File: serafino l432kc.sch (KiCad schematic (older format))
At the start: 31 parts, among them J1 USB_B_Micro, J2 Conn_01x14, J3 Conn_01x14, Q1 SI3401A-TP, SW1 SW_Push, SW2 SW_Push, U1 AP2112K-3.3, U2 USBLC6-2SC6, U3 STM32L432KCUx, Y1 32.768K

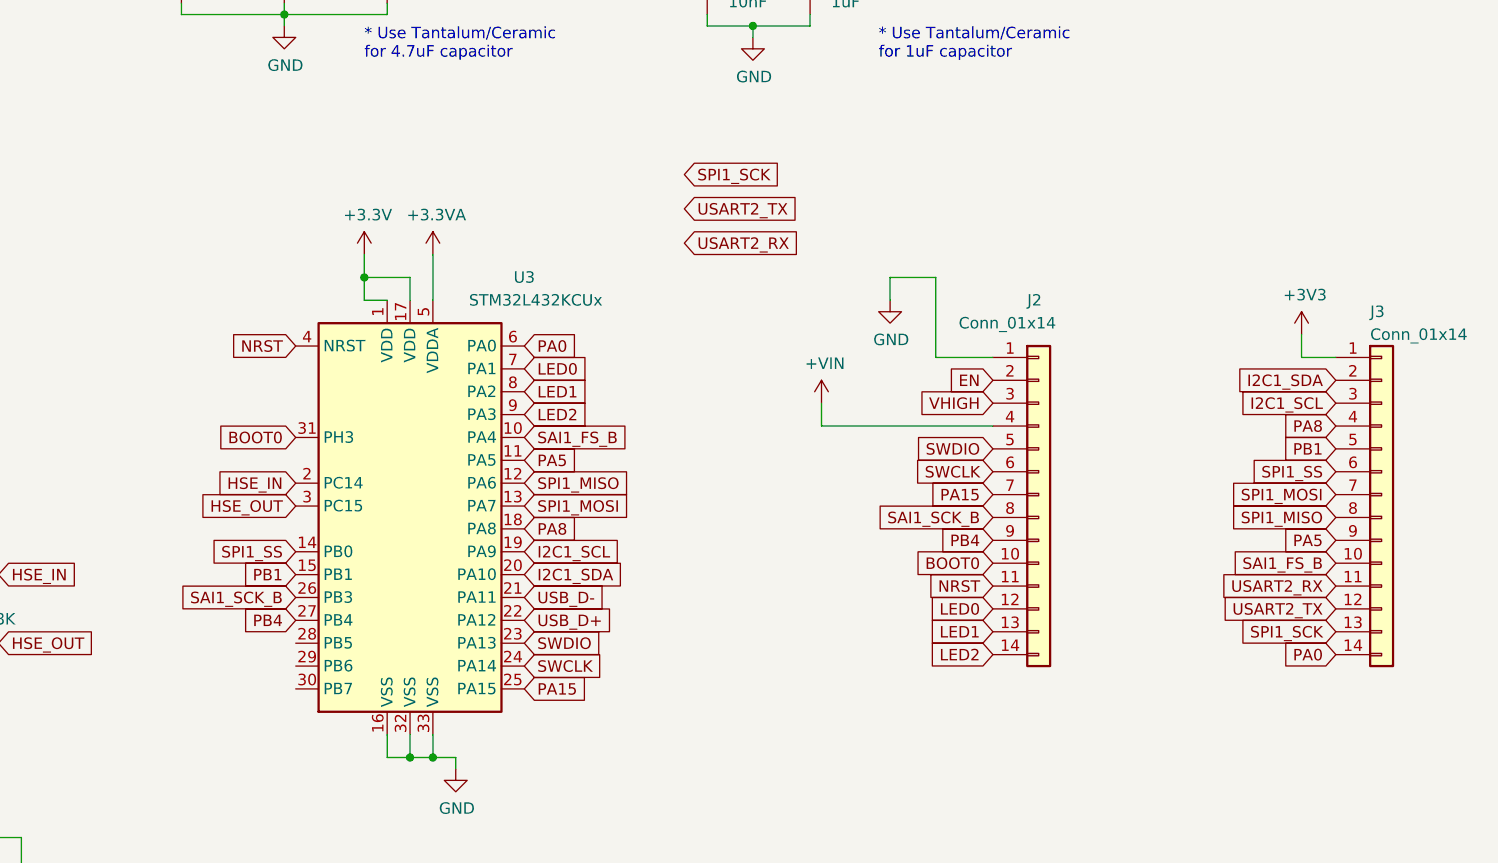
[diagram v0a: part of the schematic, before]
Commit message: PWM Leds
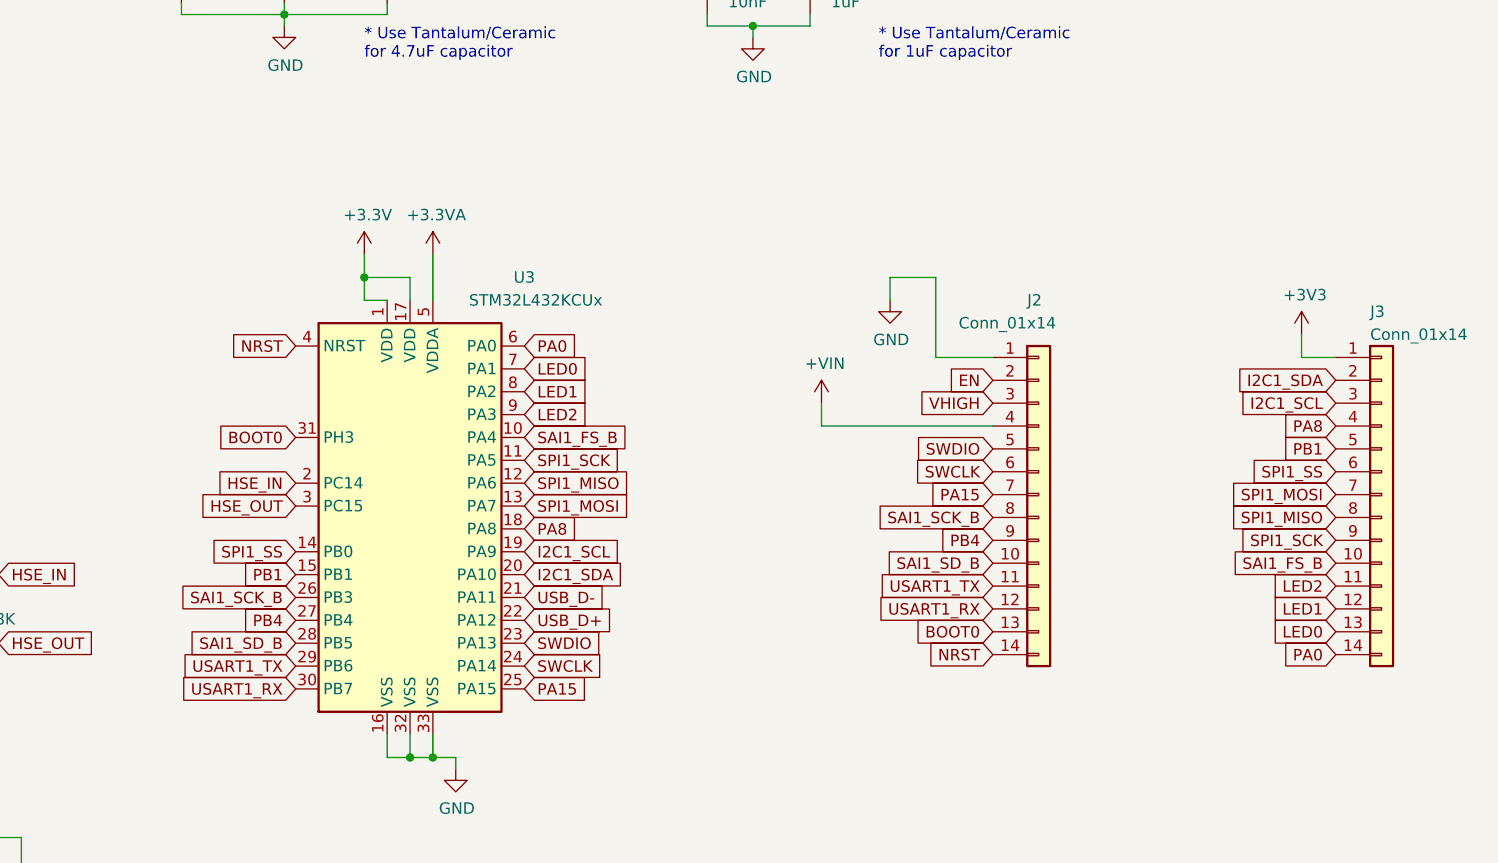
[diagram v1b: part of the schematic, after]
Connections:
- net PA5 is gone; now on net SPI1_SCK: J3.9 (Pin_9), U3.11 (PA5)
- net USART2_RX is gone; now on net LED2: J3.11 (Pin_11)
- net USART2_TX is gone; now on net LED1: J3.12 (Pin_12)
- net BOOT0: now also J2.13 (Pin_13); no longer J2.10 (Pin_10)
- net LED0: now also J3.13 (Pin_13); no longer J2.12 (Pin_12)
- net LED1: no longer J2.13 (Pin_13)
- net LED2: no longer J2.14 (Pin_14)
- net NRST: now also J2.14 (Pin_14); no longer J2.11 (Pin_11)
- net SPI1_SCK: no longer J3.13 (Pin_13)
- net SAI1_SD_B: now reaches U3.28 (PB5)
- net SAI1_SD_B: now also J2.10 (Pin_10)
- net USART1_TX: now reaches U3.29 (PB6)
- net USART1_TX: now also J2.11 (Pin_11)
- net USART1_RX: now reaches U3.30 (PB7)
- net USART1_RX: now also J2.12 (Pin_12)
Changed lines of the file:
@@
 Text GLabel 6700 4500 2    50   Input ~ 0
 USB_D-
-Text GLabel 7400 2800 2    50   Input ~ 0
-USART2_TX
-Text GLabel 7400 2950 2    50   Input ~ 0
-USART2_RX
+Text GLabel 5700 4800 0    50   Input ~ 0
+USART1_TX
+Text GLabel 5700 4900 0    50   Input ~ 0
+USART1_RX
 Text Notes 5200 1400 0    50   ~ 0
 VDD Decouples
@@
 Text GLabel 6700 4100 2    50   Input ~ 0
 SPI1_MOSI
-Text GLabel 7400 2650 2    50   Input ~ 0
+Text GLabel 6700 3900 2    50   Input ~ 0
 SPI1_SCK
 Text GLabel 6700 4000 2    50   Input ~ 0
@@
 Text GLabel 8750 3650 0    50   Input ~ 0
 VHIGH
-Text GLabel 8750 4450 0    50   Input ~ 0
+Text GLabel 8750 4750 0    50   Input ~ 0
 NRST
 Text GLabel 10250 3750 0    50   Input ~ 0
@@
 Text GLabel 8750 4250 0    50   Input ~ 0
 PB4
-Text GLabel 8750 4550 0    50   Input ~ 0
+Text GLabel 10250 4650 0    50   Input ~ 0
 LED0
-Text GLabel 8750 4650 0    50   Input ~ 0
+Text GLabel 10250 4550 0    50   Input ~ 0
 LED1
-Text GLabel 8750 4750 0    50   Input ~ 0
+Text GLabel 10250 4450 0    50   Input ~ 0
 LED2
 Text GLabel 10250 4050 0    50   Input ~ 0
@@
 Text GLabel 10250 4150 0    50   Input ~ 0
 SPI1_MISO
-Text GLabel 10250 4250 0    50   Input ~ 0
-PA5
 Text GLabel 10250 4350 0    50   Input ~ 0
 SAI1_FS_B
-Text GLabel 10250 4450 0    50   Input ~ 0
-USART2_RX
-Text GLabel 10250 4550 0    50   Input ~ 0
-USART2_TX
-Text GLabel 10250 4650 0    50   Input ~ 0
+Text GLabel 8750 4550 0    50   Input ~ 0
+USART1_RX
+Text GLabel 8750 4450 0    50   Input ~ 0
+USART1_TX
+Text GLabel 10250 4250 0    50   Input ~ 0
 SPI1_SCK
 Wire Wire Line
@@
 Wire Wire Line
 	8500 3450 8750 3450
-Text GLabel 8750 4350 0    50   Input ~ 0
+Text GLabel 8750 4650 0    50   Input ~ 0
 BOOT0
 $Comp
@@
 Wire Wire Line
 	8000 3750 8750 3750
-Text GLabel 6700 3900 2    50   Input ~ 0
-PA5
 $Comp
 L Switch:SW_Push SW2
@@
 Text Notes 8250 2150 0    50   ~ 0
 * Use Tantalum/Ceramic\nfor 1uF capacitor
+Text GLabel 5700 4700 0    50   Input ~ 0
+SAI1_SD_B
+Text GLabel 8750 4350 0    50   Input ~ 0
+SAI1_SD_B
 $EndSCHEMATC

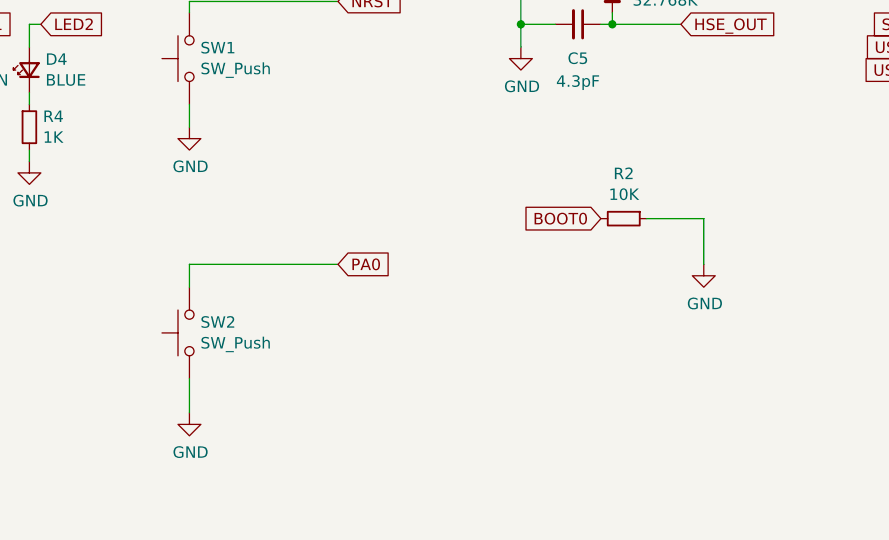
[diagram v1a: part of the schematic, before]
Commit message: BOOT0 a SW0
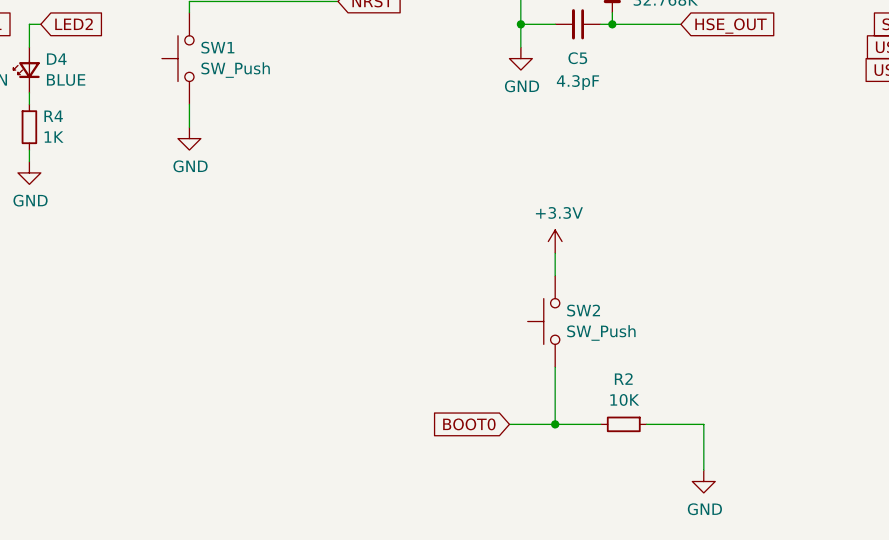
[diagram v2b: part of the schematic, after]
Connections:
- net +3V3: now also SW2.2
- net BOOT0: now also SW2.1
- net GND: no longer SW2.1
- net PA0: no longer SW2.2
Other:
- moved on the sheet: R2, SW2
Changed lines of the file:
@@
 	1    0    0    -1
 $EndComp
-Text GLabel 4050 5550 0    50   Input ~ 0
+Text GLabel 3650 6450 0    50   Input ~ 0
 BOOT0
 $Comp
 L Device:R_Small R2
 U 1 1 5FC716B0
-P 4150 5550
-F 0 "R2" V 3954 5550 50  0000 C CNN
-F 1 "10K" V 4045 5550 50  0000 C CNN
-F 2 "Resistor_SMD:R_0603_1608Metric" H 4150 5550 50  0001 C CNN
-F 3 "~" H 4150 5550 50  0001 C CNN
-F 4 "RC0603FR-0710KL" H 4150 5550 50  0001 C CNN "Part No."
-	1    4150 5550
+P 4150 6450
+F 0 "R2" V 3954 6450 50  0000 C CNN
+F 1 "10K" V 4045 6450 50  0000 C CNN
+F 2 "Resistor_SMD:R_0603_1608Metric" H 4150 6450 50  0001 C CNN
+F 3 "~" H 4150 6450 50  0001 C CNN
+F 4 "RC0603FR-0710KL" H 4150 6450 50  0001 C CNN "Part No."
+	1    4150 6450
 	0    1    1    0
 $EndComp
 Wire Wire Line
-	4250 5550 4500 5550
+	4250 6450 4500 6450
 Wire Wire Line
 	8300 3200 8300 3100
@@
 L Switch:SW_Push SW2
 U 1 1 5FF882A4
-P 2250 6050
-F 0 "SW2" V 2296 6002 50  0000 R CNN
-F 1 "SW_Push" V 2205 6002 50  0000 R CNN
-F 2 "Button_Switch_SMD:SW_Push_1P1T_NO_Vertical_Wuerth_434133025816" H 2250 6250 50  0001 C CNN
-F 3 "~" H 2250 6250 50  0001 C CNN
-F 4 "434133025816 " H 2250 6050 50  0001 C CNN "Part No."
-	1    2250 6050
-	0    -1   -1   0
-$EndComp
-Text GLabel 2900 5750 2    50   Input ~ 0
-PA0
-Wire Wire Line
-	2900 5750 2250 5750
-Wire Wire Line
-	2250 5750 2250 5850
-$Comp
-L power:GND #PWR0107
-U 1 1 5FF8C6C4
-P 2250 6400
-F 0 "#PWR0107" H 2250 6150 50  0001 C CNN
-F 1 "GND" H 2255 6227 50  0000 C CNN
-F 2 "" H 2250 6400 50  0001 C CNN
-F 3 "" H 2250 6400 50  0001 C CNN
-	1    2250 6400
-	1    0    0    -1
-$EndComp
-Wire Wire Line
-	2250 6250 2250 6400
+P 3850 6000
+F 0 "SW2" V 3896 5952 50  0000 R CNN
+F 1 "SW_Push" V 3805 5952 50  0000 R CNN
+F 2 "Button_Switch_SMD:SW_Push_1P1T_NO_Vertical_Wuerth_434133025816" H 3850 6200 50  0001 C CNN
+F 3 "~" H 3850 6200 50  0001 C CNN
+F 4 "434133025816 " H 3850 6000 50  0001 C CNN "Part No."
+	1    3850 6000
+	0    -1   -1   0
+$EndComp
 $Comp
 L power:GND #PWR0110
 U 1 1 5FF95AE4
-P 4500 5750
-F 0 "#PWR0110" H 4500 5500 50  0001 C CNN
-F 1 "GND" H 4505 5577 50  0000 C CNN
-F 2 "" H 4500 5750 50  0001 C CNN
-F 3 "" H 4500 5750 50  0001 C CNN
-	1    4500 5750
-	1    0    0    -1
-$EndComp
-Wire Wire Line
-	4500 5750 4500 5550
+P 4500 6650
+F 0 "#PWR0110" H 4500 6400 50  0001 C CNN
+F 1 "GND" H 4505 6477 50  0000 C CNN
+F 2 "" H 4500 6650 50  0001 C CNN
+F 3 "" H 4500 6650 50  0001 C CNN
+	1    4500 6650
+	1    0    0    -1
+$EndComp
+Wire Wire Line
+	4500 6650 4500 6450
 $Comp
 L serafino-l432kc-rescue:SI3401A-TP Q1
@@
 Text GLabel 8750 4350 0    50   Input ~ 0
 SAI1_SD_B
+$Comp
+L power:+3.3V #PWR?
+U 1 1 6018DE27
+P 3850 5700
+F 0 "#PWR?" H 3850 5550 50  0001 C CNN
+F 1 "+3.3V" H 3865 5873 50  0000 C CNN
+F 2 "" H 3850 5700 50  0001 C CNN
+F 3 "" H 3850 5700 50  0001 C CNN
+	1    3850 5700
+	1    0    0    -1
+$EndComp
+Wire Wire Line
+	3850 5700 3850 5800
+Wire Wire Line
+	3650 6450 3850 6450
+Wire Wire Line
+	3850 6200 3850 6450
+Connection ~ 3850 6450
+Wire Wire Line
+	3850 6450 4050 6450
 $EndSCHEMATC

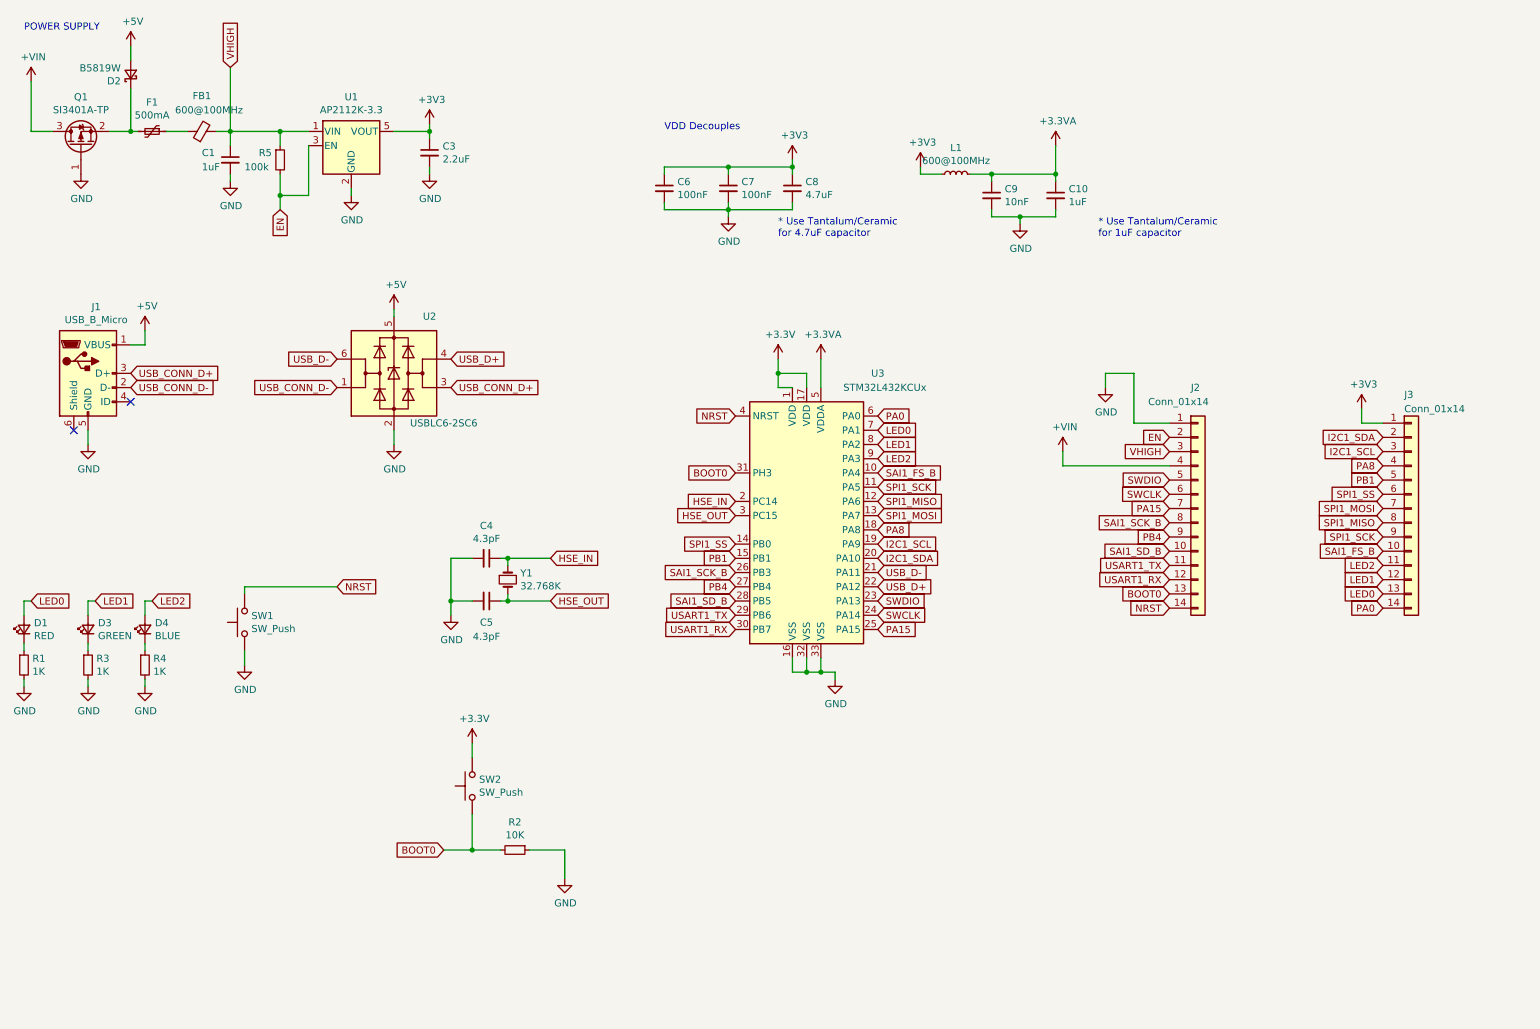
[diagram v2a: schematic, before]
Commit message: DFU LED Indicator (PA6/MISO)
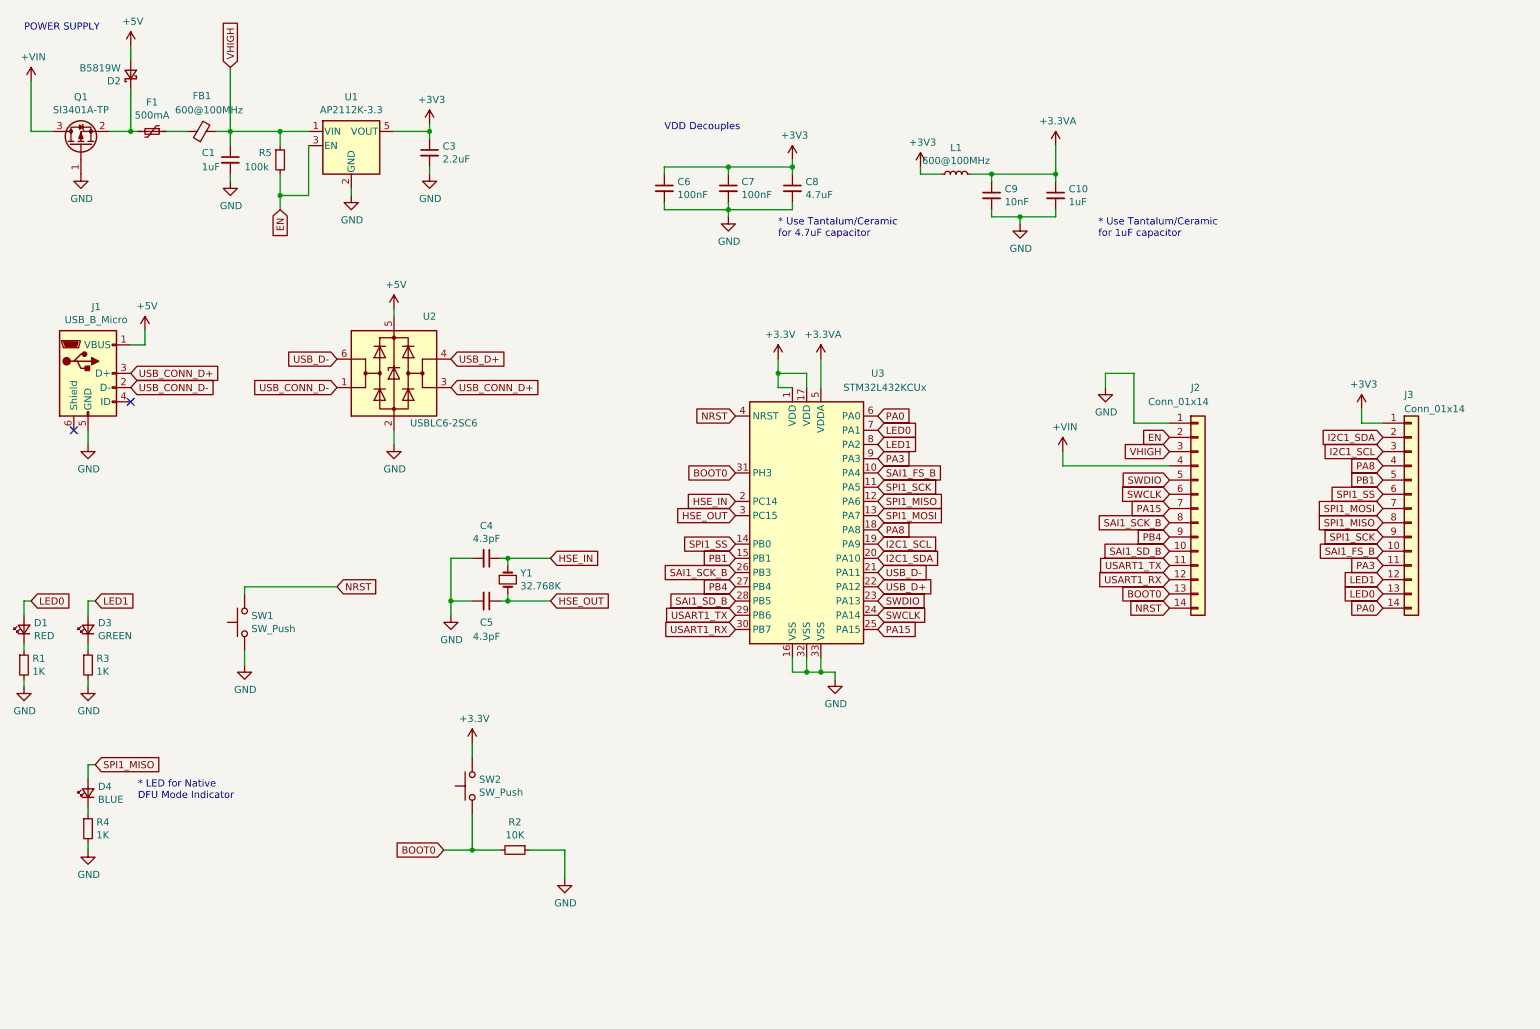
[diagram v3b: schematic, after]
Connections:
- net SPI1_MISO: now also D4.2 (A)
- net LED2 renamed PA3
- net PA3: no longer D4.2 (A)
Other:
- note added: "* LED for Native \nDFU Mode Indicator"
- moved on the sheet: D4, R4
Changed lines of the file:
@@
 $EndComp
 Text GLabel 6700 3700 2    50   Input ~ 0
-LED2
+PA3
 Text GLabel 6700 3600 2    50   Input ~ 0
 LED1
@@
 LED1
 Text GLabel 10250 4450 0    50   Input ~ 0
-LED2
+PA3
 Text GLabel 10250 4050 0    50   Input ~ 0
 SPI1_MOSI
@@
 L Device:R_Small R4
 U 1 1 5FD4ED72
-P 1550 5150
-F 0 "R4" H 1609 5196 50  0000 L CNN
-F 1 "1K" H 1609 5105 50  0000 L CNN
-F 2 "Resistor_SMD:R_0603_1608Metric" H 1550 5150 50  0001 C CNN
-F 3 "~" H 1550 5150 50  0001 C CNN
-F 4 "RC0603FR-071KL" H 1550 5150 50  0001 C CNN "Part No."
-	1    1550 5150
+P 1150 6300
+F 0 "R4" H 1209 6346 50  0000 L CNN
+F 1 "1K" H 1209 6255 50  0000 L CNN
+F 2 "Resistor_SMD:R_0603_1608Metric" H 1150 6300 50  0001 C CNN
+F 3 "~" H 1150 6300 50  0001 C CNN
+F 4 "RC0603FR-071KL" H 1150 6300 50  0001 C CNN "Part No."
+	1    1150 6300
 	1    0    0    -1
 $EndComp
@@
 L power:GND #PWR0108
 U 1 1 5FD4F1E4
-P 1550 5300
-F 0 "#PWR0108" H 1550 5050 50  0001 C CNN
-F 1 "GND" H 1555 5127 50  0000 C CNN
-F 2 "" H 1550 5300 50  0001 C CNN
-F 3 "" H 1550 5300 50  0001 C CNN
-	1    1550 5300
+P 1150 6450
+F 0 "#PWR0108" H 1150 6200 50  0001 C CNN
+F 1 "GND" H 1155 6277 50  0000 C CNN
+F 2 "" H 1150 6450 50  0001 C CNN
+F 3 "" H 1150 6450 50  0001 C CNN
+	1    1150 6450
 	1    0    0    -1
 $EndComp
@@
 L Device:LED_Small D4
 U 1 1 5FD4F3F3
-P 1550 4900
-F 0 "D4" V 1596 4830 50  0000 R CNN
-F 1 "BLUE" V 1505 4830 50  0000 R CNN
-F 2 "LED_SMD:LED_0603_1608Metric" V 1550 4900 50  0001 C CNN
-F 3 "~" V 1550 4900 50  0001 C CNN
-F 4 "155060BS75300" H 1550 4900 50  0001 C CNN "Part No."
-	1    1550 4900
+P 1150 6050
+F 0 "D4" V 1196 5980 50  0000 R CNN
+F 1 "BLUE" V 1105 5980 50  0000 R CNN
+F 2 "LED_SMD:LED_0603_1608Metric" V 1150 6050 50  0001 C CNN
+F 3 "~" V 1150 6050 50  0001 C CNN
+F 4 "155060BS75300" H 1150 6050 50  0001 C CNN "Part No."
+	1    1150 6050
 	0    -1   -1   0
 $EndComp
@@
 	1150 5000 1150 5050
 Wire Wire Line
-	1550 5000 1550 5050
+	1150 6150 1150 6200
 Wire Wire Line
 	1150 5250 1150 5300
 Wire Wire Line
-	1550 5250 1550 5300
+	1150 6400 1150 6450
 Text GLabel 1200 4700 2    50   Input ~ 0
 LED1
-Text GLabel 1600 4700 2    50   Input ~ 0
-LED2
 Wire Wire Line
 	1200 4700 1150 4700
@@
 	1150 4700 1150 4800
 Wire Wire Line
-	1600 4700 1550 4700
-Wire Wire Line
-	1550 4700 1550 4800
+	1200 5850 1150 5850
+Wire Wire Line
+	1150 5850 1150 5950
 Connection ~ 1450 1400
 Wire Wire Line
@@
 Wire Wire Line
 	3850 6450 4050 6450
+Text GLabel 1200 5850 2    50   Input ~ 0
+SPI1_MISO
+Text Notes 1500 6100 0    50   ~ 0
+* LED for Native \nDFU Mode Indicator
 $EndSCHEMATC
